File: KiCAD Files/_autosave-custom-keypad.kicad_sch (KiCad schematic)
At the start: 134 parts, among them SW1 SW_Push, SW10 SW_Push, SW11 SW_Push, SW12 SW_Push, SW13 SW_Push, SW14 SW_Push, SW15 SW_Push, SW16 SW_Push, SW17 SW_Push, SW18 SW_Push, SW19 SW_Push, SW2 SW_Push, SW20 SW_Push, SW21 SW_Push, SW22 SW_Push, SW23 SW_Push, SW24 SW_Push, SW25 SW_Push, SW26 SW_Push, SW27 SW_Push, SW28 SW_Push, SW29 SW_Push, SW3 SW_Push, SW30 SW_Push, SW31 SW_Push, SW32 SW_Push, SW33 SW_Push, SW34 SW_Push, SW35 SW_Push, SW36 SW_Push, SW37 SW_Push, SW38 SW_Push, SW39 SW_Push, SW4 SW_Push, SW40 SW_Push, SW41 SW_Push, SW42 SW_Push, SW43 SW_Push, SW44 SW_Push, SW45 SW_Push, SW46 SW_Push, SW47 SW_Push, SW48 SW_Push, SW49 SW_Push, SW5 SW_Push, SW50 SW_Push, SW51 SW_Push, SW52 SW_Push, SW53 SW_Push, SW54 SW_Push, SW55 SW_Push, SW56 SW_Push, SW57 SW_Push, SW58 SW_Push, SW59 SW_Push, SW6 SW_Push, SW60 SW_Push, SW61 SW_Push, SW62 SW_Push, SW63 SW_Push, SW64 SW_Push, SW65 SW_Push, SW66 SW_Push, SW67 SW_Push, SW7 SW_Push, SW8 SW_Push, SW9 SW_Push

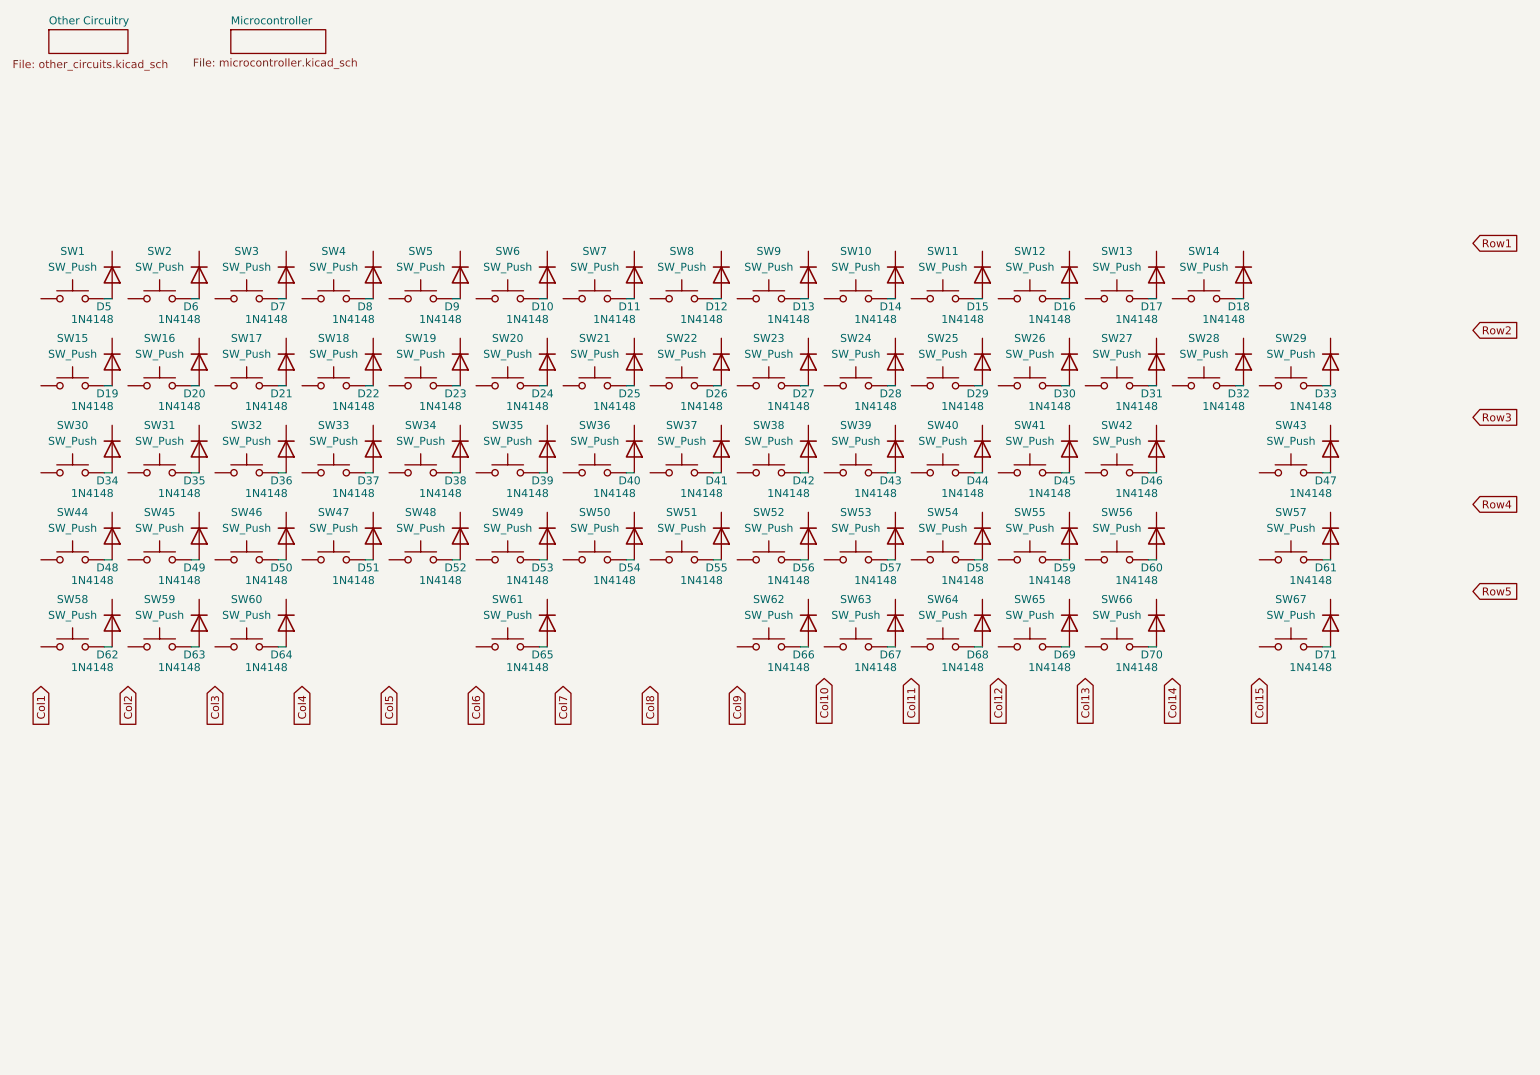
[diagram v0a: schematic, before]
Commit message: started adjusting changes for 65% keyboard
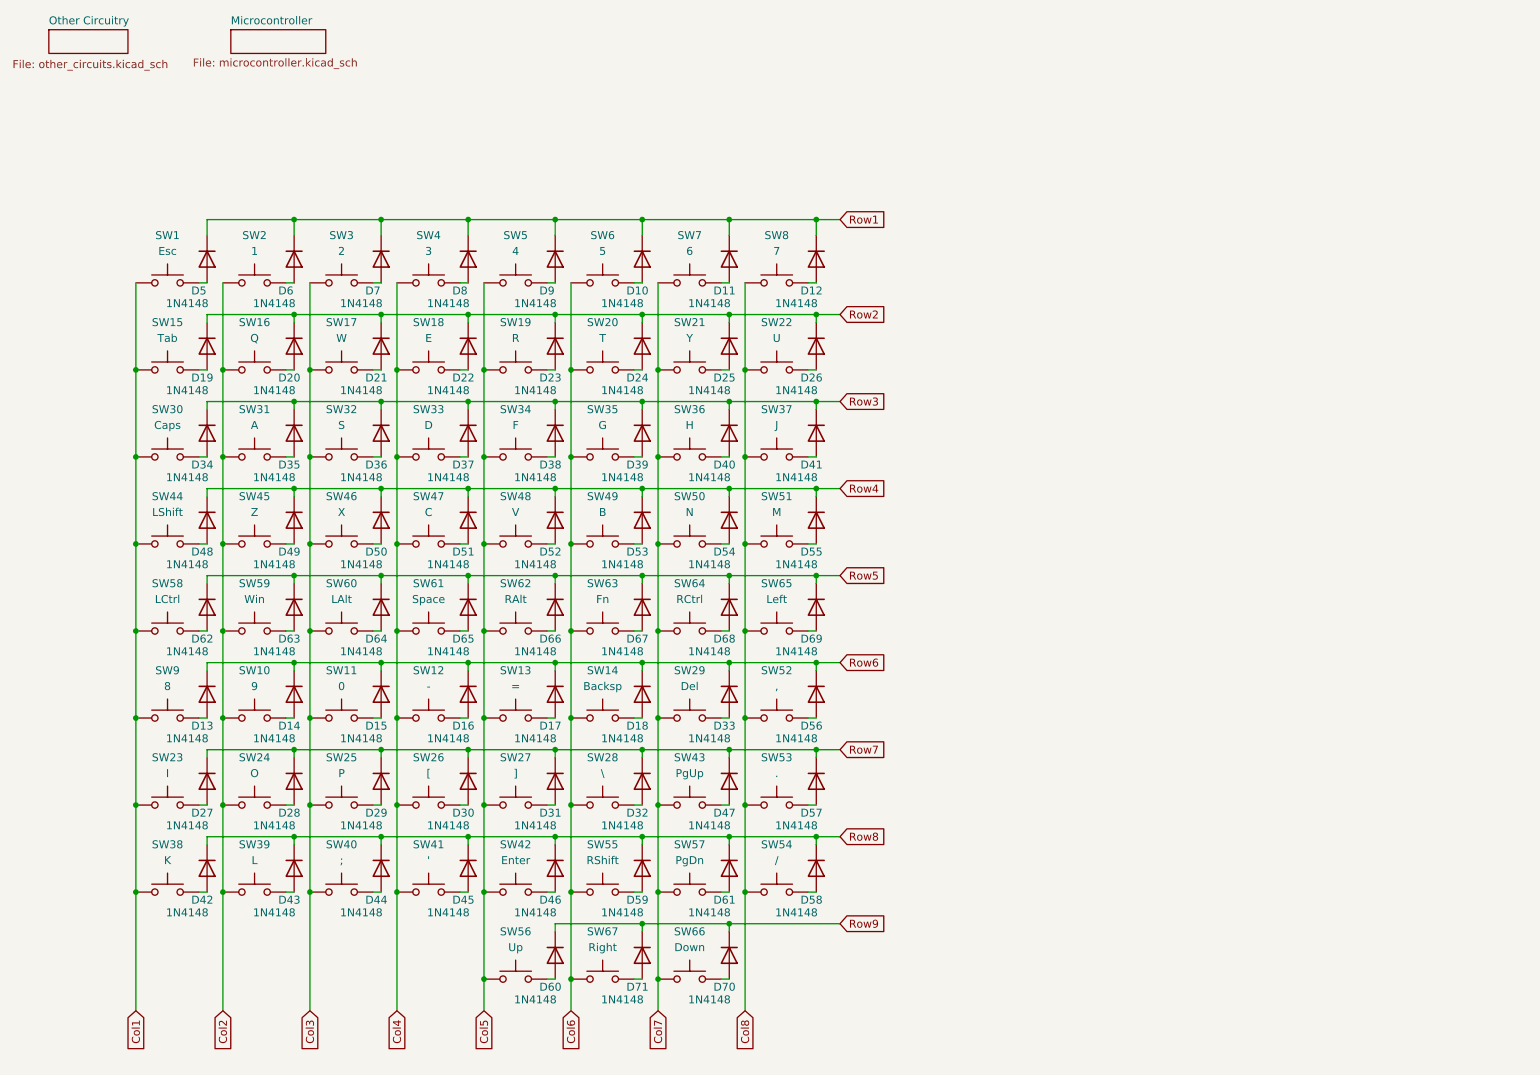
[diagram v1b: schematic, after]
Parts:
- SW1: value SW_Push -> Esc
- SW10: value SW_Push -> 9
- SW11: value SW_Push -> 0
- SW12: value SW_Push -> -
- SW13: value SW_Push -> =
- SW14: value SW_Push -> Backsp
- SW15: value SW_Push -> Tab
- SW16: value SW_Push -> Q
- SW17: value SW_Push -> W
- SW18: value SW_Push -> E
- SW19: value SW_Push -> R
- SW2: value SW_Push -> 1
- SW20: value SW_Push -> T
- SW21: value SW_Push -> Y
- SW22: value SW_Push -> U
- SW23: value SW_Push -> I
- SW24: value SW_Push -> O
- SW25: value SW_Push -> P
- SW26: value SW_Push -> [
- SW27: value SW_Push -> ]
- SW28: value SW_Push -> \
- SW29: value SW_Push -> Del
- SW3: value SW_Push -> 2
- SW30: value SW_Push -> Caps
- SW31: value SW_Push -> A
- SW32: value SW_Push -> S
- SW33: value SW_Push -> D
- SW34: value SW_Push -> F
- SW35: value SW_Push -> G
- SW36: value SW_Push -> H
- SW37: value SW_Push -> J
- SW38: value SW_Push -> K
- SW39: value SW_Push -> L
- SW4: value SW_Push -> 3
- SW40: value SW_Push -> ;
- SW41: value SW_Push -> '
- SW42: value SW_Push -> Enter
- SW43: value SW_Push -> PgUp
- SW44: value SW_Push -> LShift
- SW45: value SW_Push -> Z
- SW46: value SW_Push -> X
- SW47: value SW_Push -> C
- SW48: value SW_Push -> V
- SW49: value SW_Push -> B
- SW5: value SW_Push -> 4
- SW50: value SW_Push -> N
- SW51: value SW_Push -> M
- SW52: value SW_Push -> ,
- SW53: value SW_Push -> .
- SW54: value SW_Push -> /
- SW55: value SW_Push -> RShift
- SW56: value SW_Push -> Up
- SW57: value SW_Push -> PgDn
- SW58: value SW_Push -> LCtrl
- SW59: value SW_Push -> Win
- SW6: value SW_Push -> 5
- SW60: value SW_Push -> LAlt
- SW61: value SW_Push -> Space
- SW62: value SW_Push -> RAlt
- SW63: value SW_Push -> Fn
- SW64: value SW_Push -> RCtrl
- SW65: value SW_Push -> Left
- SW66: value SW_Push -> Down
- SW67: value SW_Push -> Right
- SW7: value SW_Push -> 6
- SW8: value SW_Push -> 7
- SW9: value SW_Push -> 8
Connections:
- net Col1: now also SW1.1, SW15.1, SW23.1, SW30.1, SW38.1, SW44.1, SW58.1, SW9.1
- net Col2: now also SW10.1, SW16.1, SW2.1, SW24.1, SW31.1, SW39.1, SW45.1, SW59.1
- net Col3: now also SW11.1, SW17.1, SW25.1, SW3.1, SW32.1, SW40.1, SW46.1, SW60.1
- net Col4: now also SW12.1, SW18.1, SW26.1, SW33.1, SW4.1, SW41.1, SW47.1, SW61.1
- net Col5: now also SW13.1, SW19.1, SW27.1, SW34.1, SW42.1, SW48.1, SW5.1, SW56.1, SW62.1
- net Col6: now also SW14.1, SW20.1, SW28.1, SW35.1, SW49.1, SW55.1, SW6.1, SW63.1, SW67.1
- net Col7: now also SW21.1, SW29.1, SW36.1, SW43.1, SW50.1, SW57.1, SW64.1, SW66.1, SW7.1
- net Col8: now also SW22.1, SW37.1, SW51.1, SW52.1, SW53.1, SW54.1, SW65.1, SW8.1
- net Row1: now also D10.1 (K), D11.1 (K), D12.1 (K), D5.1 (K), D6.1 (K), D7.1 (K), D8.1 (K), D9.1 (K)
- net Row2: now also D19.1 (K), D20.1 (K), D21.1 (K), D22.1 (K), D23.1 (K), D24.1 (K), D25.1 (K), D26.1 (K)
- net Row3: now also D34.1 (K), D35.1 (K), D36.1 (K), D37.1 (K), D38.1 (K), D39.1 (K), D40.1 (K), D41.1 (K)
- net Row4: now also D48.1 (K), D49.1 (K), D50.1 (K), D51.1 (K), D52.1 (K), D53.1 (K), D54.1 (K), D55.1 (K)
- net Row5: now also D62.1 (K), D63.1 (K), D64.1 (K), D65.1 (K), D66.1 (K), D67.1 (K), D68.1 (K), D69.1 (K)
- net Row6: now reaches D14.1 (K)
- net Row6: now also D13.1 (K), D15.1 (K), D16.1 (K), D17.1 (K), D18.1 (K), D33.1 (K), D56.1 (K)
- net Row7: now reaches D27.1 (K)
- net Row7: now also D28.1 (K), D29.1 (K), D30.1 (K), D31.1 (K), D32.1 (K), D47.1 (K), D57.1 (K)
- net Row8: now reaches D43.1 (K)
- net Row8: now also D42.1 (K), D44.1 (K), D45.1 (K), D46.1 (K), D58.1 (K), D59.1 (K), D61.1 (K)
- net Row9: now reaches D60.1 (K)
- net Row9: now also D70.1 (K), D71.1 (K)
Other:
- moved on the sheet: D10, D11, D12, D13, D14, D15, D16, D17, D18, D19, D20, D21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
